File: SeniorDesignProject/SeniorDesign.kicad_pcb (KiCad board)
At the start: 2 copper layers, 69.1 x 65.3 mm, 32 parts, among them J1 RJ45(LoadCells), J2 RJ45(Accelerometer), J3 PICkit3, J5 ID-12LA Header, J6 XBEE Header, J7 7-Segment Display, P7 Power 1, U1 INA827, U2 LM1117-3.3, U3 ICL7660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

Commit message: Fixed copper pour
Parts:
- removed the G*** at (170.8, 69.0)
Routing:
- added copper zone on F.Cu, net GND
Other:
- board outline removed

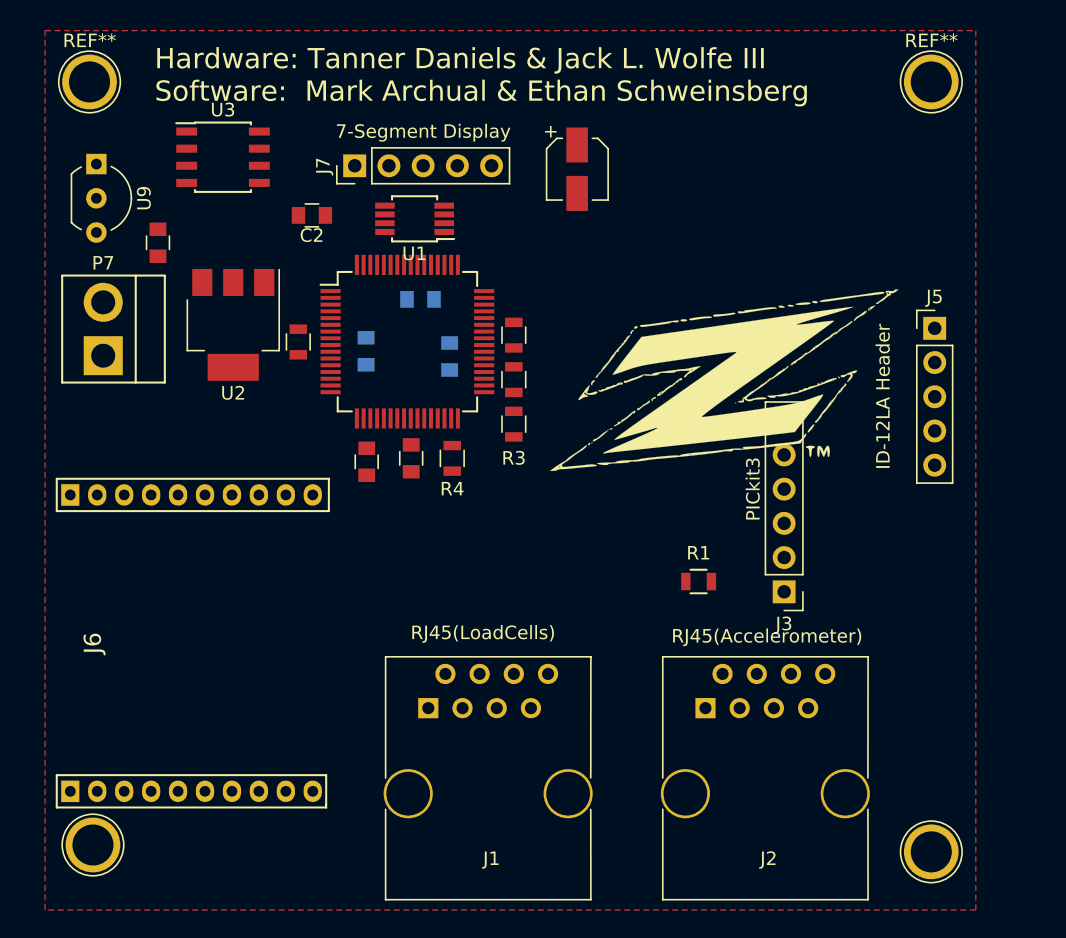
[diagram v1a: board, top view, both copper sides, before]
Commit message: Routed main board, still need to ad LED indicaters
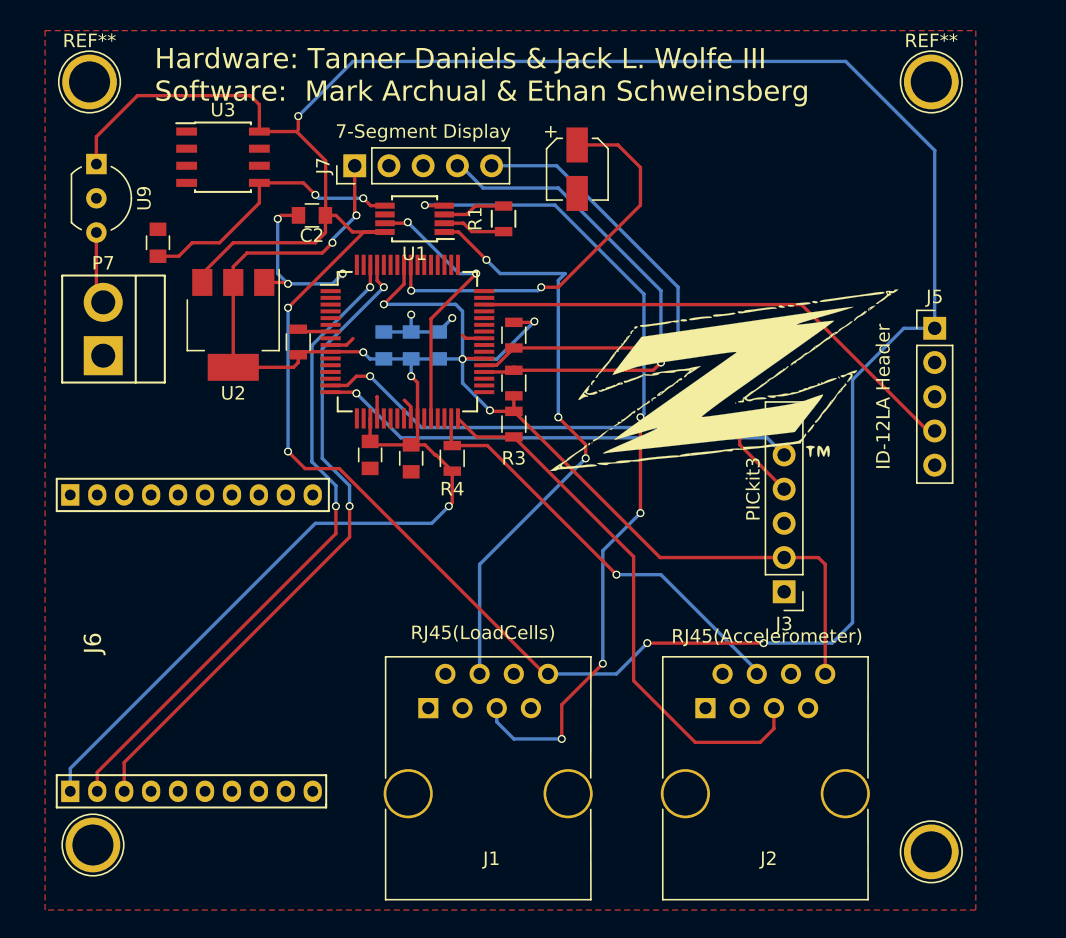
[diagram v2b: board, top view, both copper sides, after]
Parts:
- moved R1 30.6 mm to (150.9, 70.4), turned to 90 degrees
- moved C7 3.49 mm to (144.0, 79.8), turned to 90 degrees
- moved C5 1.39 mm to (142.0, 79.8)
- moved C6 1.16 mm to (146.1, 79.8)
- moved C4 0.57 mm to (141.0, 87.9), turned to 270 degrees
- moved R5 0.25 mm to (151.6, 82.5)
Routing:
- net +5V: track 0.00 -> 206.9 mm, vias 0 -> 5
- net 3.3V: track 0.51 -> 163.1 mm, vias 0 -> 9
- net A+: track 0.00 -> 62.4 mm, vias 0 -> 5
- net UART2TX: track 0.00 -> 48.9 mm, vias 0 -> 2
- net UART2RX: track 0.00 -> 48.9 mm, vias 0 -> 2
- net A-: track 0.00 -> 44.3 mm, vias 0 -> 3
- net SCL2: track 0.00 -> 40.8 mm
- net PGED3: track 0.00 -> 37.9 mm, vias 0 -> 2
- net SDA1: track 0.00 -> 37.8 mm, vias 0 -> 1
- net UART1RX: track 0.00 -> 37.3 mm
- net SCL1: track 0.00 -> 36.7 mm, vias 0 -> 1
- net PGEC3: track 0.00 -> 35.6 mm, vias 0 -> 1
- net SDA2: track 0.00 -> 31.9 mm, vias 0 -> 1
- net Net-(C8-Pad1): track 0.00 -> 29.8 mm, vias 0 -> 2
- net GND: track 0.00 -> 26.8 mm, vias 0 -> 5
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
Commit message: Changed accelerometer to SPI rather than I2C
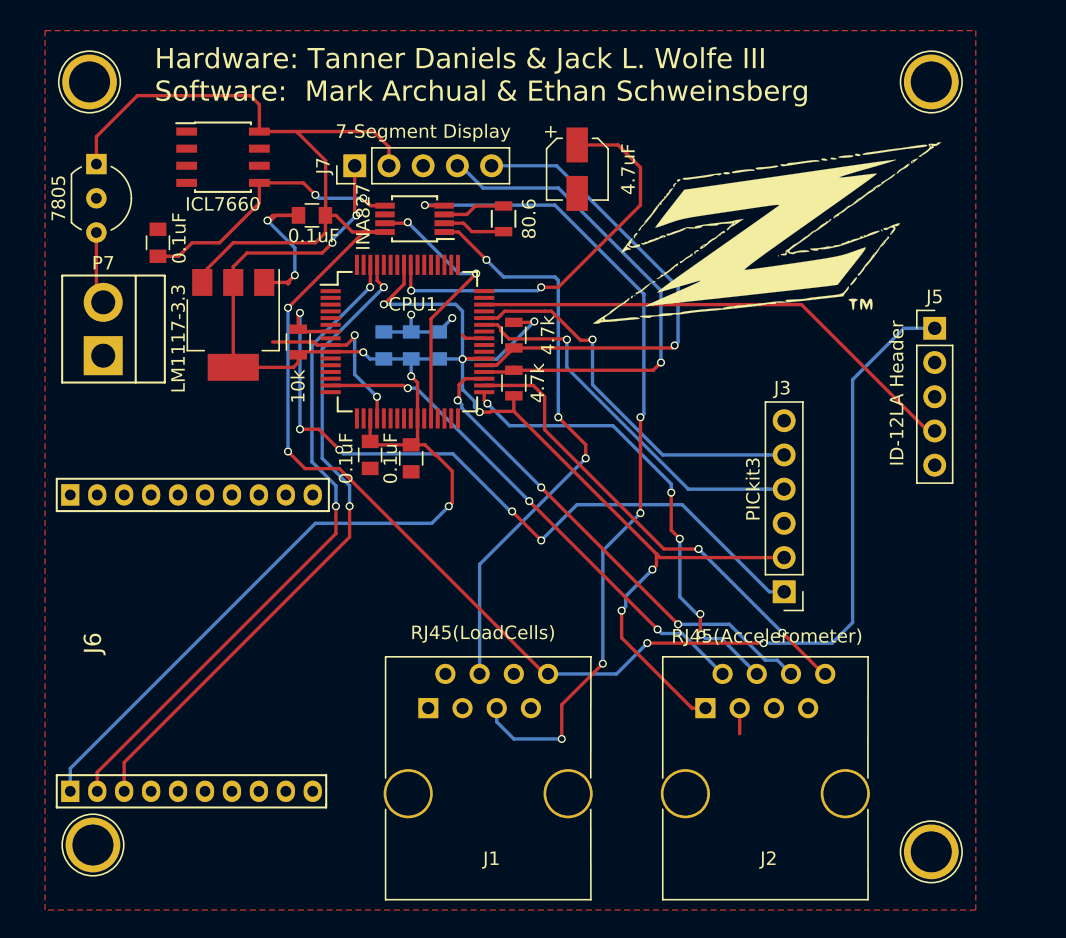
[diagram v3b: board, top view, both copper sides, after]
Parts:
- removed R3, R4: 4.7k, Resistors_SMD:R_0805
- moved G*** 11.4 mm to (170.3, 71.4)
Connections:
- CPU1 pad 15: PGED3 -> SS1
- CPU1 pad 16: PGEC3 -> Net-(CPU1-Pad16)
- CPU1 pad 31: SDA2 -> Net-(CPU1-Pad31)
- CPU1 pad 32: SCL2 -> Net-(CPU1-Pad32)
- CPU1 pad 33: Net-(CPU1-Pad33) -> SDO1
- CPU1 pad 34: Net-(CPU1-Pad34) -> SDI1
- CPU1 pad 35: Net-(CPU1-Pad35) -> SCK1
- CPU1 pad 43: Net-(CPU1-Pad43) -> PGED2
- CPU1 pad 44: Net-(CPU1-Pad44) -> PGEC2
- CPU1 pad 7: Net-(CPU1-Pad7) -> MCLR
- J2 pad 1: Net-(J2-Pad1) -> 3.3V
- J2 pad 2: Net-(J2-Pad2) -> SS1
- J2 pad 3: Net-(J2-Pad3) -> GND
- J2 pad 4: SDA2 -> SDO1
- J2 pad 5: SCL2 -> Net-(J2-Pad5)
- J2 pad 6: Net-(J2-Pad6) -> SCK1
- J2 pad 7: GND -> Net-(J2-Pad7)
- J2 pad 8: 3.3V -> SDI1
- J3 pad 4: PGED3 -> PGED2
- J3 pad 5: PGEC3 -> PGEC2
- J7 pad 2: +5V(2) -> +5V
- J7 pad 3: GND(2) -> GND
- R2 pad 2: Net-(CPU1-Pad7) -> MCLR
- U9 pad 1: +5V -> (no net)
- U9 pad 2: GND -> (no net)
- U9 pad 3: +9V -> (no net)
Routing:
- net +5V: track 206.9 -> 149.8 mm, vias 5 -> 4
- net MCLR: track 0.00 -> 55.5 mm, vias 0 -> 5
- net SCL2: track 40.8 -> 0.00 mm
- net SS1: track 0.00 -> 38.0 mm, vias 0 -> 3
- net PGED3: track 37.9 -> 0.00 mm, vias 2 -> 0
- net SCK1: track 0.00 -> 36.6 mm, vias 0 -> 3
- net SDI1: track 0.00 -> 35.6 mm, vias 0 -> 2
- net PGEC3: track 35.6 -> 0.00 mm, vias 1 -> 0
- net SDO1: track 0.00 -> 34.9 mm, vias 0 -> 5
- net SDA2: track 31.9 -> 0.00 mm, vias 1 -> 0
- net PGEC2: track 0.00 -> 28.9 mm, vias 0 -> 1
- net PGED2: track 0.00 -> 28.7 mm, vias 0 -> 1
- net GND: track 26.8 -> 37.0 mm, vias 5 -> 6
- net 3.3V: track 163.1 -> 168.0 mm, vias 9 -> 11
- net Net-(CPU1-Pad7): track 2.47 -> 0.00 mm
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
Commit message: Updates to accelerometer board and main board
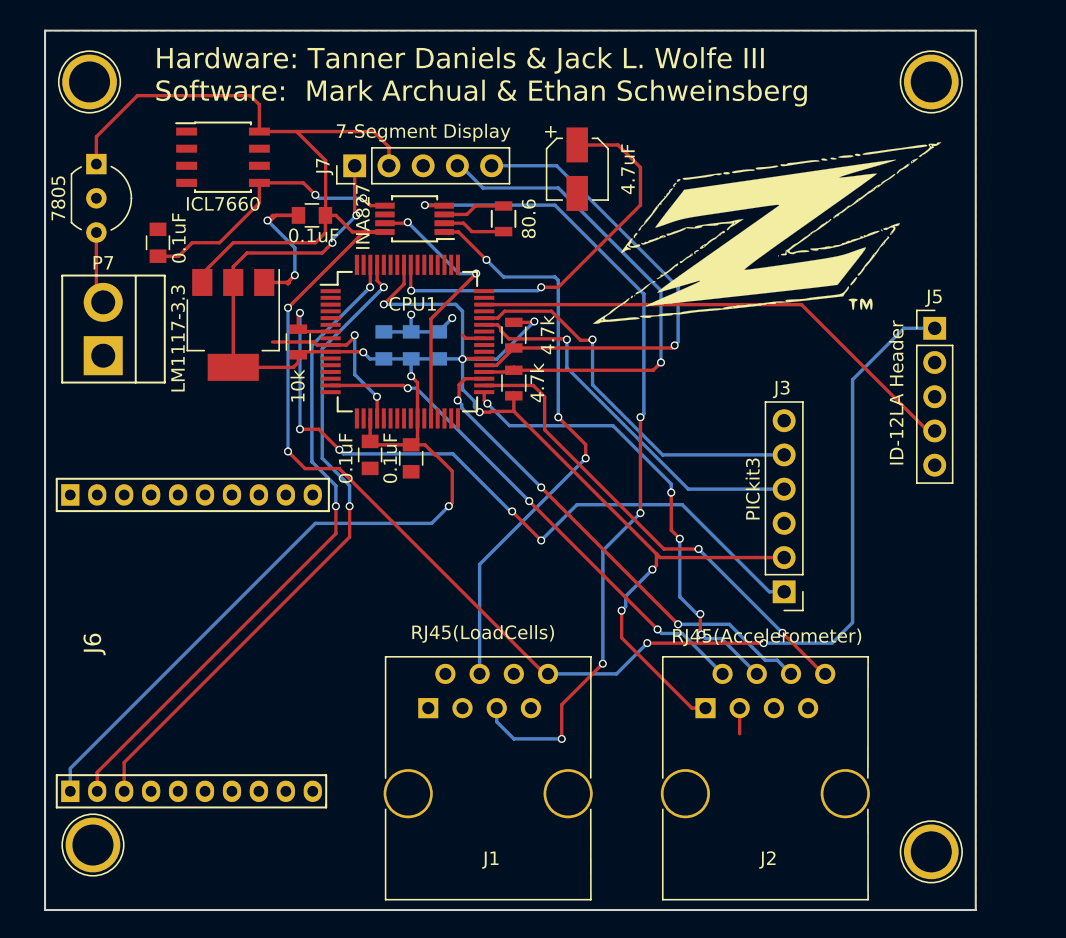
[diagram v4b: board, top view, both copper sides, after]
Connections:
- net SDI1 renamed MISO1
- net SDO1 renamed MOSI1
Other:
- board outline added: 69.1 x 65.3 mm
- rule trace_min: 0.2 -> 0.1524
- rule via_min_size: 0.4 -> 0.3302

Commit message: Updates to main board
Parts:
- added C10: 10u, Capacitors_THT:CP_Radial_D5.0mm_P2.00mm, F.Cu at (121.4, 77.2)
- added C9: 10u, Capacitors_THT:CP_Radial_D5.0mm_P2.00mm, F.Cu at (119.4, 71.4)
- C8: footprint Capacitors_SMD:CP_Elec_4x4.5 -> Capacitors_THT:CP_Radial_D5.0mm_P2.00mm
- moved P7 6.00 mm to (120.9, 86.5)
- moved U9 3.14 mm to (123.7, 65.5), turned to 180 degrees
- moved C8 2.42 mm to (158.8, 66.8), turned to 90 degrees
- moved ? 1.61 mm to (118.9, 117.3)
- moved REF** 1.27 mm to (118.9, 60.2)
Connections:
- net MISO1 renamed MISO
- net MOSI1 renamed MOSI
- net SCK1 renamed SCK
- net SS1 renamed SS
- CPU1 pad 47: Net-(CPU1-Pad47) -> LED
- CPU1 pad 49: Net-(CPU1-Pad49) -> CP
- U9 pad 1: (no net) -> +5V
- U9 pad 2: (no net) -> GND
- U9 pad 3: (no net) -> +9V
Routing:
- net CP: track 0.00 -> 46.0 mm, vias 0 -> 4
- net LED: track 0.00 -> 36.5 mm
- net GND: track 37.3 -> 56.1 mm, vias 6 -> 7
- net +9V: track 5.39 -> 20.0 mm
- net Net-(C9-Pad1): track 0.00 -> 11.1 mm
- net 3.3V: track 168.0 -> 175.8 mm, vias 11 -> 10
- net Net-(C9-Pad2): track 0.00 -> 7.46 mm
- net Net-(C8-Pad1): track 29.8 -> 23.2 mm
- net -5V: track 20.7 -> 27.0 mm
- net +5V: track 149.8 -> 145.8 mm
- net PGED2: track 28.7 -> 29.4 mm
- net PGEC2: track 28.9 -> 29.5 mm
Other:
- board size 69.1 x 65.3 mm -> 69.8 x 63.5 mm

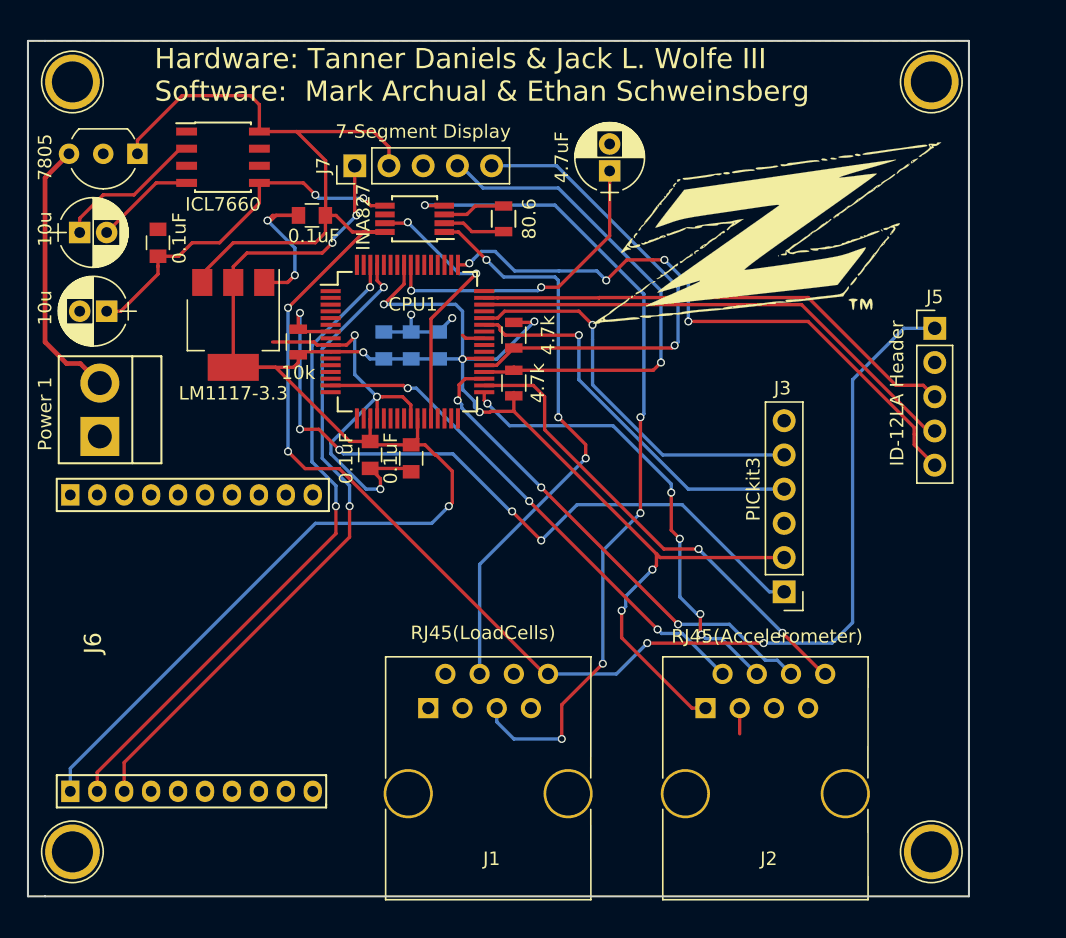
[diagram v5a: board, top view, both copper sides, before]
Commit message: Re routed traces added tantalum cap for vcap
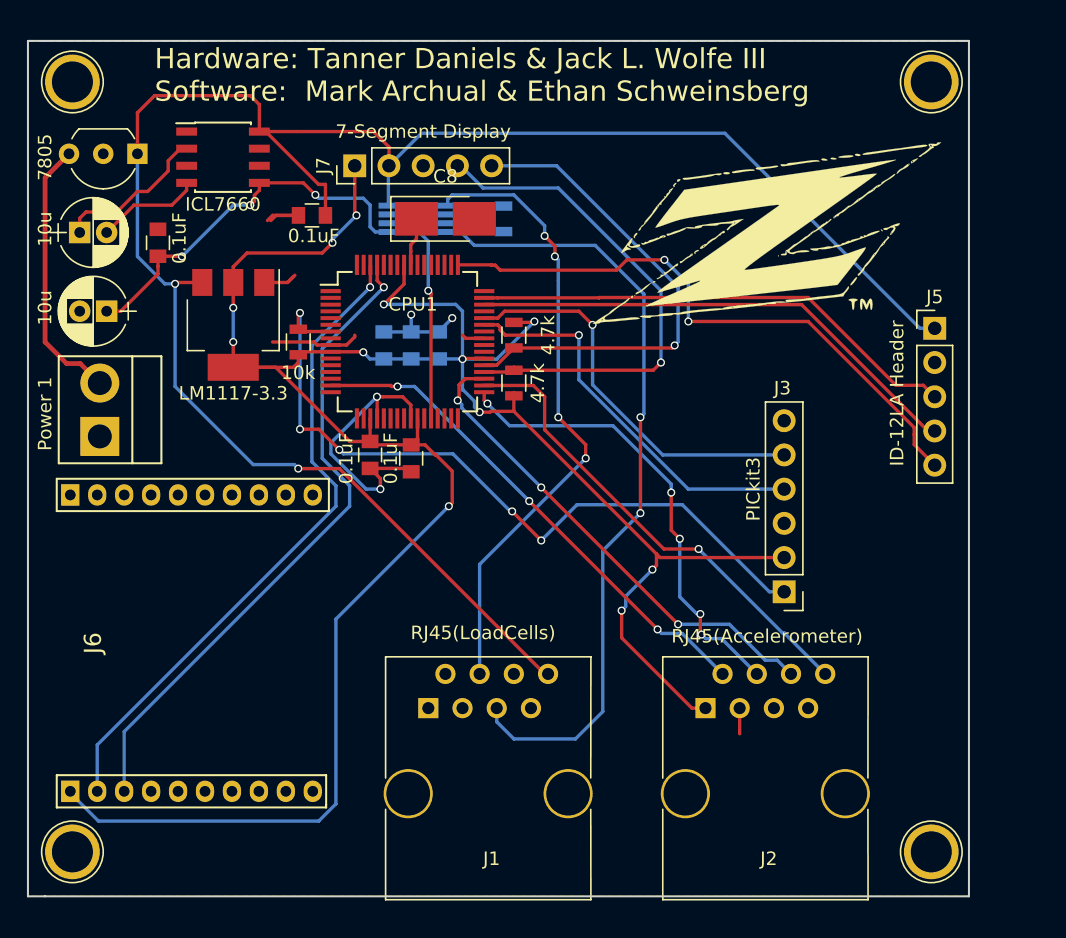
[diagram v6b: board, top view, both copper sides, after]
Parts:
- C8: value 4.7uF -> 10uF; footprint Capacitors_THT:CP_Radial_D5.0mm_P2.00mm -> Capacitors_Tantalum_SMD:CP_Tantalum_Case-T_EIA-3528-12_Hand
- R1, U1: moved to B.Cu
- moved C8 12.7 mm to (146.6, 70.4), turned to 0 degrees
- moved U1 0.25 mm to (144.5, 70.4)
- turned R1 to 270 degrees
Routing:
- net Net-(C8-Pad1): track 23.2 -> 3.59 mm, vias 2 -> 0
- net GND: track 56.1 -> 45.9 mm, vias 7 -> 4
- net 3.3V: track 175.8 -> 184.7 mm, vias 10 -> 12
- net A+: track 62.4 -> 59.0 mm, vias 5 -> 2
- net A-: track 43.3 -> 46.6 mm, vias 3 -> 4
- net AN13: track 20.5 -> 17.9 mm, vias 2 -> 1
- net +5V: track 145.8 -> 143.8 mm, vias 4 -> 2
- net -5V: track 27.0 -> 28.7 mm, vias 2 -> 3
- net CP: track 46.0 -> 44.6 mm, vias 4 -> 2
- net MISO: track 35.6 -> 35.7 mm, vias 2 -> 1
- net UART2TX: vias 2 -> 1
- net UART2RX: vias 2 -> 1

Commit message: Updates (Final design)
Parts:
- added C11: .33uF, Capacitors_THT:CP_Radial_D5.0mm_P2.00mm, F.Cu at (119.6, 77.2)
- added C12: .1uF, Capacitors_THT:CP_Radial_D5.0mm_P2.00mm, F.Cu at (119.6, 71.4)
- added C13: 10uF, Capacitors_Tantalum_SMD:CP_Tantalum_Case-T_EIA-3528-12_Hand, B.Cu at (129.7, 78.2)
- added C14: 10uF, Capacitors_Tantalum_SMD:CP_Tantalum_Case-T_EIA-3528-12_Hand, B.Cu at (129.7, 82.0)
- C10, C9: value 10u -> 10uF
- moved C10 14.5 mm to (134.9, 71.9)
- moved C1 11.5 mm to (135.9, 67.8), turned to 180 degrees
- moved C9 7.60 mm to (127.0, 71.9)
- moved C2 5.32 mm to (135.1, 65.0), turned to 270 degrees
- moved U2 3.21 mm to (129.8, 81.3)
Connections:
- U2 pad 1: GND -> Net-(C13-Pad2)
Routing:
- net -5V: track 28.7 -> 13.9 mm, vias 3 -> 0
- net GND: track 45.9 -> 35.6 mm
- net Net-(C13-Pad2): track 0.00 -> 8.39 mm, vias 0 -> 1
- net Net-(C9-Pad1): track 11.6 -> 8.42 mm
- net Net-(C9-Pad2): track 7.78 -> 5.36 mm
- net +9V: track 20.0 -> 18.6 mm
- net +5V: track 143.8 -> 143.0 mm, vias 2 -> 1
- net 3.3V: track 184.7 -> 184.1 mm, vias 12 -> 9
